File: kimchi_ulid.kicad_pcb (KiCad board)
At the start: 4 copper layers, 209.3 x 89.3 mm, 21 parts, among them J1 DF40HC(3.5)-60DS, J2 DF40HC(3.5)-60DS, J3 KUSBX-AS1N-B, J4 54-00176, J5 SGTL5000XNLA3, SW1 TL3301NF260QG, SW2 TL3301NF260QG, SW3 TL3301NF260QG, SW4 TL3301NF260QG, SW5 TL3301NF260QG, SW6 TL3301NF260QG, SW7 TL3301NF260QG, SW8 TL3301NF260QG, U1 24C32

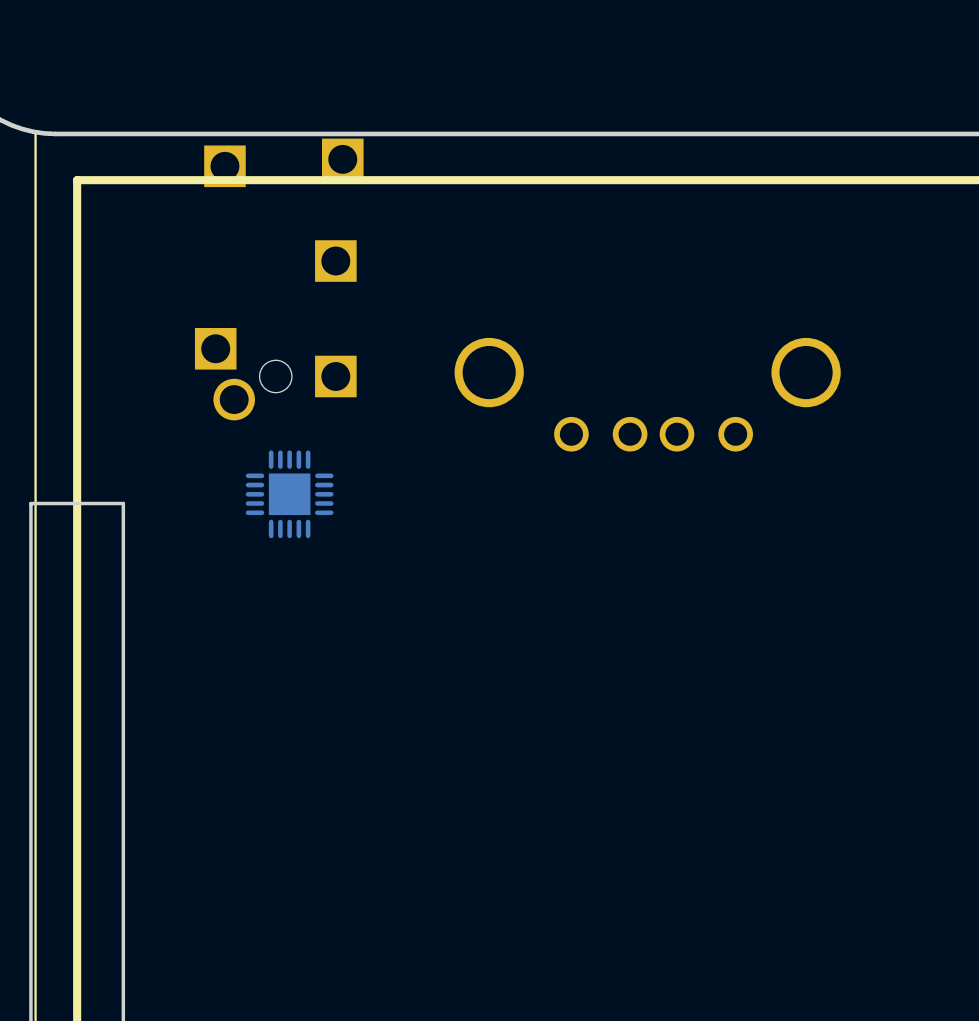
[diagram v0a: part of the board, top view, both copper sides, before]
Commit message: Oscillator Circuit
Oscillator circuit and related components added to the codec circuit. These may be unnecessary but are pending review.
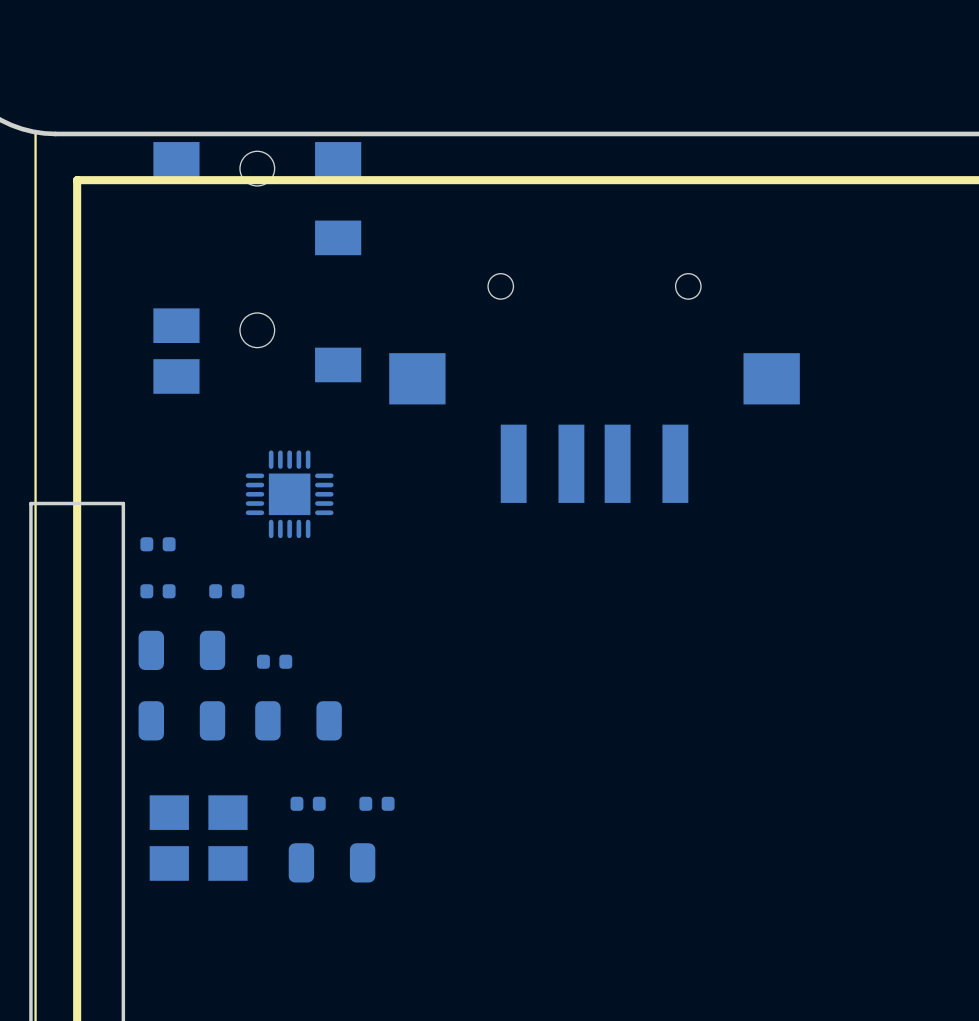
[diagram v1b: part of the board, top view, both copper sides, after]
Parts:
- added C1: C0402C104K9PACTU, kimchi_ulid:C0402, B.Cu at (83.0, 99.0)
- added C2: C0402C104K9PACTU, kimchi_ulid:C0402, B.Cu at (76.5, 89.8)
- added C3: C0402C104K9PACTU, kimchi_ulid:C0402, B.Cu at (81.5, 92.8)
- added C4: C0402C104K9PACTU, kimchi_ulid:C0402, B.Cu at (86.0, 99.0)
- added C5: C0402C104K9PACTU, kimchi_ulid:C0402, B.Cu at (79.5, 89.8)
- added C6: T491A105K010AT, kimchi_ulid:C1206, B.Cu at (77.5, 95.4)
- added C7: T491A105K010AT, kimchi_ulid:C1206, B.Cu at (84.0, 101.6)
- added C8: T491A105K010AT, kimchi_ulid:C1206, B.Cu at (77.5, 92.4)
- added C9: T491A105K010AT, kimchi_ulid:C1206, B.Cu at (82.6, 95.4)
- added R1: RC0402JR-072K2L, AVR-KiCAD-Lib-Resistors:R0402, B.Cu at (76.5, 87.8)
- added X1: ASFL1-12.288MHZ-EC-T, kimchi_ulid:ASFL1, B.Cu at (78.3, 100.5)
- J3: value KUSBX-AS1N-B -> 1-292303-6; footprint kimchi_ulid:USB_A -> kimchi_ulid:TE_1-292303-6
- J4: value 54-00176 -> 54-00177; footprint kimchi_ulid:54-00176 -> kimchi_ulid:54-00177
- moved J3 6.48 mm to (95.4, 76.6)
- moved J4 1.28 mm to (80.8, 69.0)
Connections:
- J4 pad 1: Net-(J4-Pad1) -> HPOUT_L
- J4 pad 4: Net-(J4-Pad4) -> GND
- J4 pad 6: Net-(J4-Pad6) -> HPOUT_R
- J5 pad 1: Net-(J5-Pad1) -> HPOUT_L
- J5 pad 10: Net-(J5-Pad10) -> MIC_IN
- J5 pad 11: Net-(J5-Pad11) -> MIC_BIAS
- J5 pad 12: Net-(J5-Pad12) -> VDD_3V3
- J5 pad 2: Net-(J5-Pad2) -> GND
- J5 pad 20: Net-(J5-Pad20) -> VDD_3V3
- J5 pad 21: Net-(J5-Pad21) -> GND
- J5 pad 3: Net-(J5-Pad3) -> VDD_3V3
- J5 pad 4: Net-(J5-Pad4) -> HPOUT_R

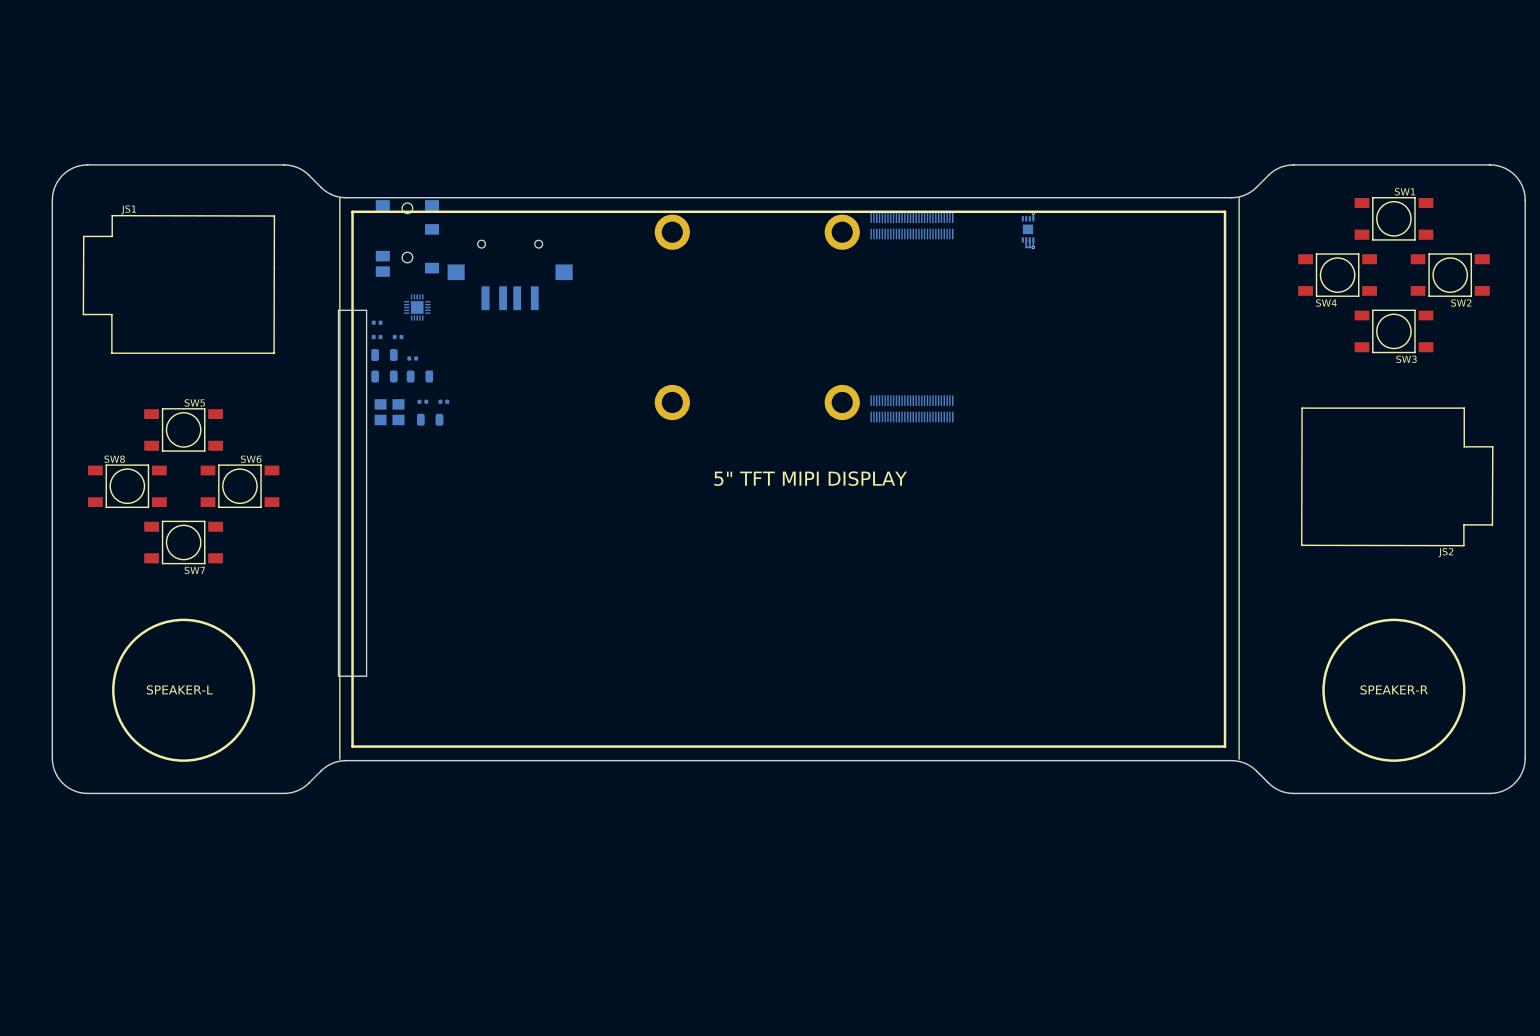
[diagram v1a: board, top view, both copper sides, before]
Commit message: Design Refactor and Major Progress
Refactored the design of the lid, integrated the schematics from the Display lid, and the HiFi lid. Changed PCB shape to reflect change to dual screen design. Found SPI TFT display for bottom display. Library updated with component footprints for new parts, and library errors and issues from importing parts from other projects resolved.
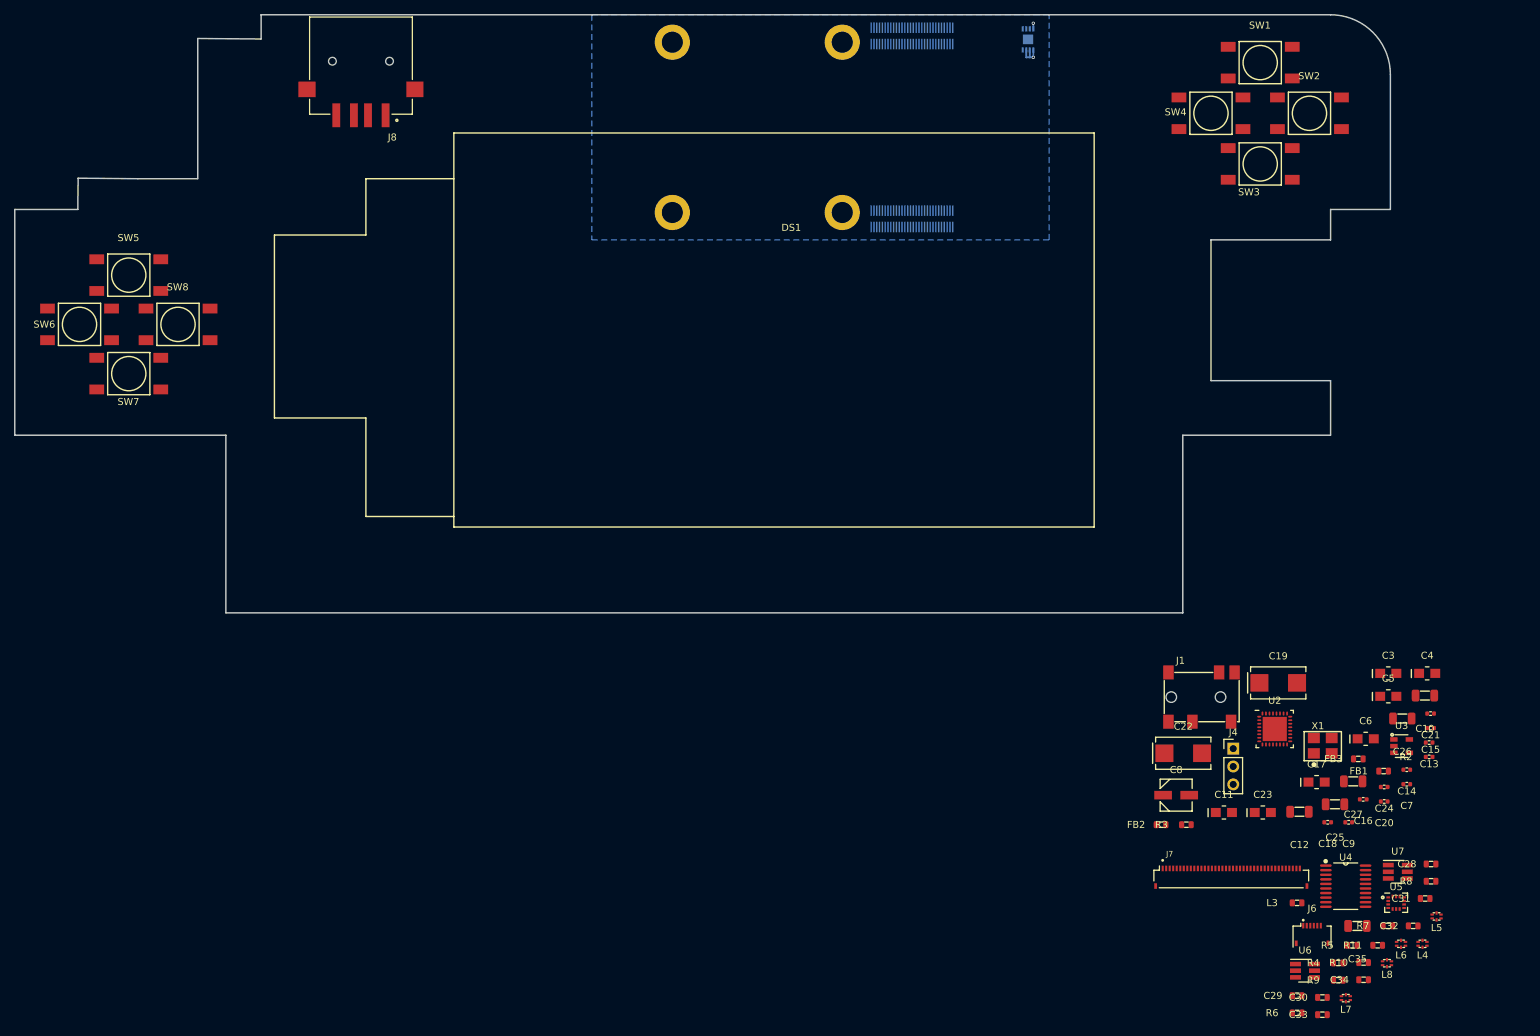
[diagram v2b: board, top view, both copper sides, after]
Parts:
- removed C1, C2: C0402C104K9PACTU, kimchi_ulid:C0402
- removed the J3 at (95.4, 76.6)
- removed J5: SGTL5000XNLA3, kimchi_ulid:QFN40P300X300X60-21N
- removed JS1, JS2: Keyes_HW-504, kimchi_ulid:Keyes_JoyStick
- removed R1: RC0402JR-072K2L, AVR-KiCAD-Lib-Resistors:R0402
- added C10: T491A105K010AT, kimchi_ulid:C1206, F.Cu at (225.4, 140.8)
- added C11: T494A106M006AT, kimchi_ulid:T494A106M006AT, F.Cu at (196.8, 157.4)
- added C12: T491A105K010AT, kimchi_ulid:C1206, F.Cu at (207.6, 157.3)
- added C13: C0402C104K9PACTU, kimchi_ulid:C0402, F.Cu at (226.0, 147.4)
- added C14: C0402C104K9PACTU, kimchi_ulid:C0402, F.Cu at (222.8, 151.3)
- added C15: C0402C104K9PACTU, kimchi_ulid:C0402, F.Cu at (226.2, 145.4)
- added C16: C0402C104K9PACTU, kimchi_ulid:C0402, F.Cu at (216.6, 155.5)
- added C17: T494A106M006AT, kimchi_ulid:T494A106M006AT, F.Cu at (210.0, 153.1)
- added C18: C0402C104K9PACTU, kimchi_ulid:C0402, F.Cu at (211.6, 158.8)
- added C19: T491D227M010AT, kimchi_ulid:T491D227M010AT, F.Cu at (204.6, 138.9)
- added C20: C0402C104K9PACTU, kimchi_ulid:C0402, F.Cu at (219.6, 155.8)
- added C21: C0402C104K9PACTU, kimchi_ulid:C0402, F.Cu at (226.2, 143.3)
- added C22: T491D227M010AT, kimchi_ulid:T491D227M010AT, F.Cu at (191.1, 148.9)
- added C23: T494A106M006AT, kimchi_ulid:T494A106M006AT, F.Cu at (202.4, 157.4)
- added C24: C0402C104K9PACTU, kimchi_ulid:C0402, F.Cu at (219.6, 153.7)
- added C25: T491A105K010AT, kimchi_ulid:C1206, F.Cu at (212.6, 156.2)
- added C26: T491A105K010AT, kimchi_ulid:C1206, F.Cu at (222.2, 144.0)
- added C27: T491A105K010AT, kimchi_ulid:C1206, F.Cu at (215.2, 152.9)
- added C28: C0603C104M5RACAUTO, kimchi_ulid:C0603, F.Cu at (226.3, 164.7)
- added C29: C0603C104M5RACAUTO, kimchi_ulid:C0603, F.Cu at (207.2, 183.4)
- added C30: C0603C104M5RACAUTO, kimchi_ulid:C0603, F.Cu at (210.8, 183.7)
- added C31: CL10A106MP8NNNC, kimchi_ulid:C0603, F.Cu at (225.4, 169.6)
- added C32: C0603C105K4PAC7411, kimchi_ulid:C0603, F.Cu at (223.7, 173.5)
- added C33: CGA3E3X7R1H224K080AB, kimchi_ulid:C0603, F.Cu at (210.8, 186.1)
- added C34: C0603C104M5RACAUTO, kimchi_ulid:C0603, F.Cu at (216.7, 181.1)
- added C35: CC1206MKX5R5BB107, kimchi_ulid:C1206, F.Cu at (215.8, 173.5)
- added DS1: ER-TFT035-6, kimchi_ulid:ER-TFT035-6_LCD_DISPLAY, F.Cu at (135.4, 88.8)
- added FB1: FBMJ1608HM180NTR, kimchi_ulid:R0603, F.Cu at (219.5, 151.5)
- added FB2: FBMJ1608HM180NTR, kimchi_ulid:R0603, F.Cu at (187.9, 159.1)
- added FB3: FBMJ1608HM180NTR, kimchi_ulid:R0603, F.Cu at (215.9, 149.8)
- added J1: 54-00177, kimchi_ulid:54-00177, F.Cu at (186.9, 141.0)
- added J6: H19C-6S-0.5SH, kimchi_ulid:HRS_FH19C-6S-0.5SH_1x06-1MP_P0.50mm, F.Cu at (209.4, 174.7)
- added J7: FH19C-40S-0.5SH(10), kimchi_ulid:HRS_FH19C-40S-0.5SH_1x40-1MP_P0.50mm, F.Cu at (197.9, 166.6)
- added J8: 1-292303-6, kimchi_ulid:TE_1-292303-6, F.Cu at (74.2, 50.6)
- added L1: GG_LOGO, kimchi_ulid:groupgets_logo, B.Cu at (66.8, 124.2)
- added L2: OSHPARK_LOGO, kimchi_ulid:oshpark_logo, B.Cu at (75.6, 124.4)
- added L3: TYA4012220M-10, kimchi_ulid:R0603, F.Cu at (207.2, 170.2)
- added L4: LCFE121002, kimchi_ulid:LCFE121002, F.Cu at (225.1, 176.0)
- added L5: LCFE121002, kimchi_ulid:LCFE121002, F.Cu at (227.1, 172.1)
- added L6: LCFE121002, kimchi_ulid:LCFE121002, F.Cu at (222.0, 176.0)
- added L7: LCFE121002, kimchi_ulid:LCFE121002, F.Cu at (214.2, 183.8)
- added L8: LCFE121002, kimchi_ulid:LCFE121002, F.Cu at (220.0, 178.8)
- added R10: RC0603JR-074K7L, kimchi_ulid:R0603, F.Cu at (216.7, 178.7)
- added R11: RE0603FRE0710RL, kimchi_ulid:R0603, F.Cu at (218.7, 176.2)
- added R2: RC0402JR-072K2L, AVR-KiCAD-Lib-Resistors:R0402, F.Cu at (226.0, 149.5)
- added R3: RC0603FR-0747KL, AVR-KiCAD-Lib-Resistors:R0603, F.Cu at (191.5, 159.1)
- added R4: RC0603JR-074K7L, kimchi_ulid:R0603, F.Cu at (213.1, 178.8)
- added R5: RC0603JR-074K7L, kimchi_ulid:R0603, F.Cu at (215.1, 176.2)
- added R6: RC0603JR-074K7L, kimchi_ulid:R0603, F.Cu at (207.2, 185.9)
- added R7: RC0603JR-074K7L, kimchi_ulid:R0603, F.Cu at (220.1, 173.5)
- added R8: RC0603JR-074K7L, kimchi_ulid:R0603, F.Cu at (226.3, 167.1)
- added R9: RC0603JR-074K7L, kimchi_ulid:R0603, F.Cu at (213.1, 181.2)
- added U2: WM8750CJLGEFL, kimchi_ulid:QFN-32_EP_5x5_Pitch0.5mm, F.Cu at (204.1, 145.5)
- added U3: SN74LV1T34DBVRG4, kimchi_ulid:SOT-23-5, F.Cu at (222.1, 147.9)
- added U4: TXS0108EPW, kimchi_ulid:TXS0108EPWR, F.Cu at (214.1, 167.8)
- added U5: LSM6DSRTR, kimchi_ulid:LSM6DSRTR, F.Cu at (221.3, 170.2)
- added U6: AP3019AKTR-G1, TO_SOT_Packages_SMD:SOT-23-6_Handsoldering, F.Cu at (208.4, 179.9)
- added U7: TPD3S014, TO_SOT_Packages_SMD:SOT-23-6_Handsoldering, F.Cu at (221.6, 165.8)
- C3, C4, C5: value C0402C104K9PACTU -> T494A106M006AT; footprint kimchi_ulid:C0402 -> kimchi_ulid:T494A106M006AT; moved to F.Cu
- C6: value T491A105K010AT -> T494A106M006AT; footprint kimchi_ulid:C1206 -> kimchi_ulid:T494A106M006AT; moved to F.Cu
- C7, C9: value T491A105K010AT -> C0402C104K9PACTU; footprint kimchi_ulid:C1206 -> kimchi_ulid:C0402; moved to F.Cu
- C8: value T491A105K010AT -> UZP1H0R1MCL1GB; footprint kimchi_ulid:C1206 -> kimchi_ulid:UZP1H0R1MCL1GB; moved to F.Cu
- J4: value 54-00177 -> Conn_01x03_Male; footprint kimchi_ulid:54-00177 -> Pin_Headers:Pin_Header_Straight_1x03_Pitch2.54mm; moved to F.Cu
- X1: moved to F.Cu
- moved C5 149.7 mm to (220.2, 140.9)
- moved C6 148.7 mm to (217.0, 146.9)
- moved C7 148.1 mm to (222.8, 153.4)
- moved C9 146.4 mm to (214.6, 158.8)
- moved C3 145.7 mm to (220.2, 137.6)
- moved C4 145.0 mm to (225.7, 137.6)
- moved J4 141.6 mm to (198.2, 148.3), turned to 0 degrees
- moved X1 140.8 mm to (210.9, 147.9)
- moved C8 128.7 mm to (190.1, 154.9)
- moved LOGO1 58.1 mm to (59.2, 124.2)
- moved SW6 32.4 mm to (34.2, 88.0)
- moved SW2 30.5 mm to (209.0, 58.0)
- moved SW3 30.5 mm to (202.0, 65.2)
- moved SW1 29.2 mm to (202.0, 50.8)
- moved SW4 29.2 mm to (195.0, 58.0)
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- renumbered H3 to H2, H2 to H3, J1 to J2, J2 to J3
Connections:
- C5 pad 1: VDD_3V3 -> VDDA
- C6 pad 1: MIC_IN -> VDD
- C6 pad 2: Net-(C6-Pad2) -> GND
- C7 pad 1: MIC_BIAS -> VDD
- C8 pad 1: Net-(C8-Pad1) -> VDDA
- C8 pad 2: SPEAKER_L -> GND
- C9 pad 1: Net-(C9-Pad1) -> MIC_BIAS
- C9 pad 2: SPEAKER_R -> GND
- J4 pad 1: HPOUT_L -> SAI3_MCLK
- J4 pad 3: Net-(J4-Pad3) -> MCLK
- X1 pad 4: VDD_3V3 -> VDD
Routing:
- added copper zone on B.Cu, net GND
- added copper zone on In1.Cu, net GND
- added copper zone on In2.Cu, net VDD_3V3
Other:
- board size 209.3 x 89.3 mm -> 195.5 x 85 mm
- board text removed: "5" TFT MIPI DISPLAY"
- board text removed: "LITHIUM POLYMER BATTERY"
- board text removed: "SPEAKER-L"
- board text removed: "SPEAKER-R"

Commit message: Two Projects
Created a dedicated project for the upper screen PCB, I moved the IMU and USB A host circuits to their own schematic page and made them part of the PCB project for the bottom half PCB that holds the SPI touch screen, controls, battery, and Kimchi module.
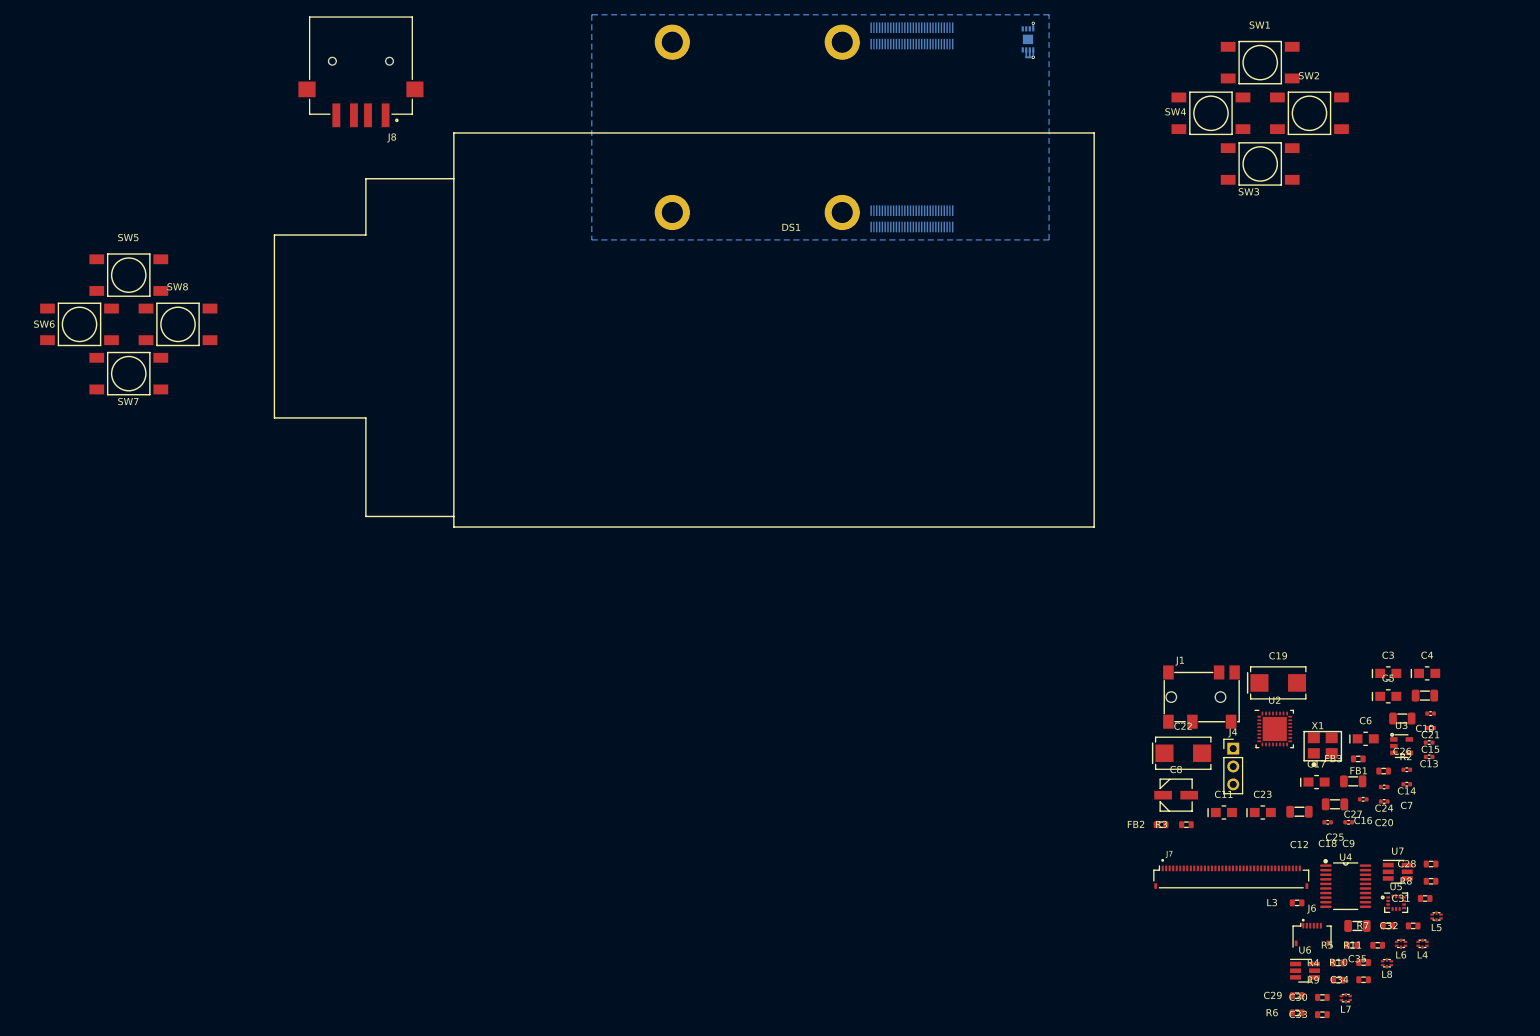
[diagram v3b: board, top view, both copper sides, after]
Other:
- board outline removed
